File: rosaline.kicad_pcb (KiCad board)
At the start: 2 copper layers, 285.4 x 94.9 mm, 147 parts, among them J1 USB, J2 AVR_ISP_6, J3 JST, SW1 RESET, SW2 BOOT, U1 ATMEGA328-PU, Y1 16MHz

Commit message: Rename project
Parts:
- 1.75u_MX3: value Caps -> Esc
- moved Flags 5.00 mm to (244.1, 146.7)
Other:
- board text added: "Rosaline rev1.1 u/peejeh 08/2021"
- board text removed: "Juliet rev1 u/peejeh 05/2021"
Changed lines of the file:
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@@
   (page A4)
   (title_block
-    (title "Juliet PCB")
+    (title "Rosaline PCB")
     (date 2021-01-23)
     (rev 1)
@@
   (module juliet:MX_PCB_700H (layer F.Cu)
     (at 152.4 140.49375)
-    (fp_text reference 7u_MX30 (at -1.905 3.095625) (layer F.Cu)
+    (fp_text reference 7u_MX30 (at -1.905 3.095625) (layer F.SilkS)
       (effects (font (size 1.27 1.524) (thickness 0.2032)))
     )
-    (fp_text value Space (at -0.238125 5.000625) (layer F.Cu)
+    (fp_text value Space (at -0.238125 5.000625) (layer F.SilkS)
       (effects (font (size 1.27 1.524) (thickness 0.2032)))
     )
@@
   (module juliet:MX (layer F.Cu)
     (at 147.6375 140.49375)
-    (fp_text reference 1u_MX30 (at -7.62 3.095625) (layer F.SilkS)
+    (fp_text reference 1u_MX30 (at -7.62 3.095625) (layer F.Mask)
       (effects (font (size 1.27 1.524) (thickness 0.2032)))
     )
-    (fp_text value Fn2 (at -4.7625 5.000625) (layer F.SilkS)
+    (fp_text value Fn2 (at -4.7625 5.000625) (layer F.Mask)
       (effects (font (size 1.27 1.524) (thickness 0.2032)))
     )
@@
       (effects (font (size 1.27 1.524) (thickness 0.2032)))
     )
-    (fp_text value Caps (at 0 5.08) (layer F.Mask)
+    (fp_text value Esc (at 0 5.08) (layer F.Mask)
       (effects (font (size 1.27 1.524) (thickness 0.2032)))
     )
@@
   )
   (module juliet:Flags (layer B.Cu)
-    (at 249.07875 146.685 180)
+    (at 244.078125 146.685 180)
     (fp_text reference Flags (at 0 4.4) (layer B.SilkS) hide
       (effects (font (size 1 1) (thickness 0.15)) (justify mirror))
@@
     (arrow2b (pts (xy 9.884735 36.344325) (xy 11.010753 35.756973)))
   )
-  (gr_text "Juliet rev1 u/peejeh 05/2021" (at 292.893996 147.042311) (layer B.Mask)
+  (gr_text "Rosaline rev1.1 u/peejeh 08/2021" (at 292.893996 147.042311) (layer B.Mask)
     (effects (font (size 1.5 1.5) (thickness 0.3)) (justify left mirror))
   )

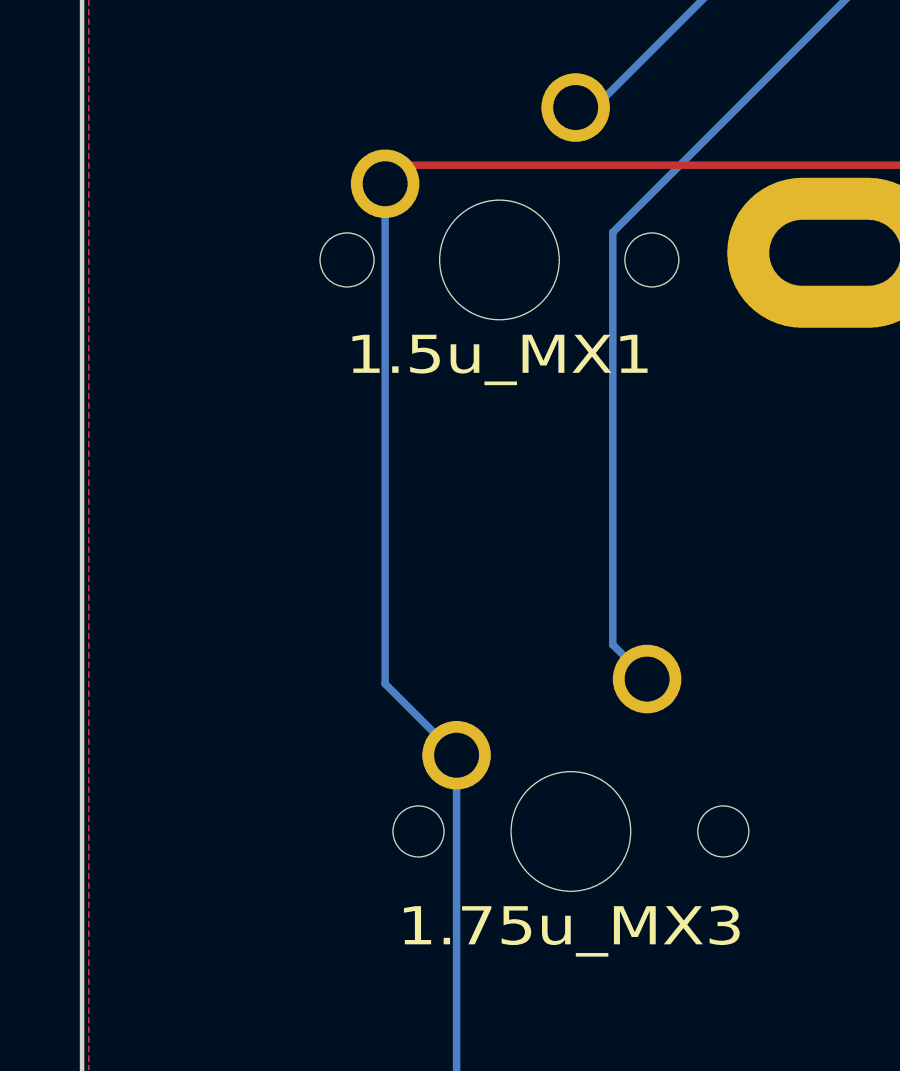
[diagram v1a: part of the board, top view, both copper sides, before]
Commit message: Add stepped caps lock switch footprint
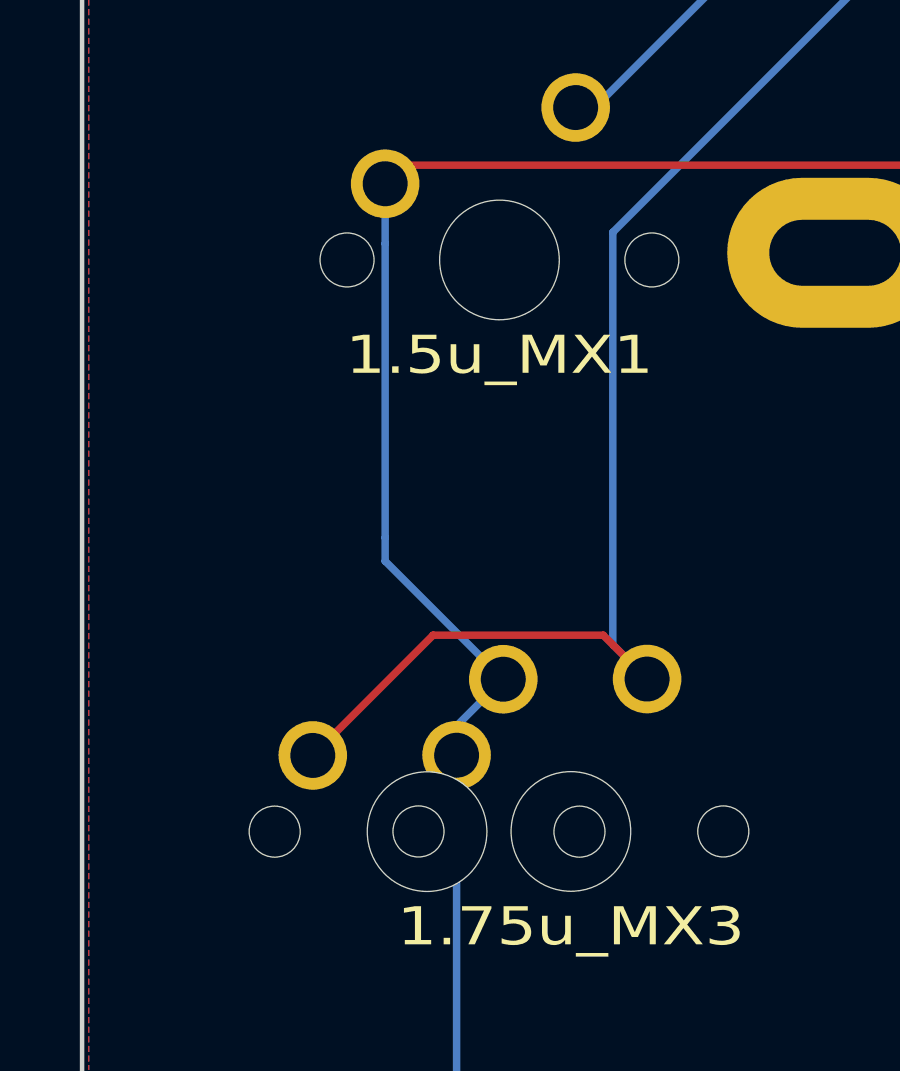
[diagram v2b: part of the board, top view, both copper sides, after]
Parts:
- added stepped_MX3: Esc, juliet:MX, F.Cu at (21.4, 102.4)
- 1.5u_MX46: value Backspace -> Back
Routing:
- net Net-(1.75u_MX3-Pad1): track 33.6 -> 47.0 mm
- net /COL0: track 256.4 -> 257.7 mm
